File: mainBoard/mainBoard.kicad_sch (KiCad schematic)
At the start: 0 parts

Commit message: Added Stuff
Added Microcontroller, keyboard pins, voltage regulator, programming pins, and resonator.
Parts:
- added C1: 100nF, symbol Device:C_Small
- added C2, C6, C7: 10µF, symbol Device:C_Small
- added C4, C5: 22pF, symbol Device:C_Small
- added J2: Programmer, symbol Connector:Conn_01x05_Pin
- added J3: Keyboard, symbol Connector:Conn_01x05_Pin
- added U1: STM32G030K8Tx, Package_QFP:LQFP-32_7x7mm_P0.8mm, symbol MCU_ST_STM32G0:STM32G030K8Tx
- added U2: AMS1117-3.3, Package_TO_SOT_SMD:SOT-223-3_TabPin2, symbol Regulator_Linear:AMS1117-3.3
- added Y1: 48MHz, symbol Device:Crystal
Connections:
- new net: C4.2, U1.2 (PC14), Y1.2
- new net: C5.2, U1.3 (PC15), Y1.1
- new net +3V3: C1.1, C2.1, C6.1, J2.5 (Pin_5), J3.1 (Pin_1), U1.4 (VDD), U2.2 (VO)
- new net +5V: C7.1, U2.3 (VI)
- new net CS: J3.3 (Pin_3), U1.11 (PA4)
- new net GND: C1.2, C2.2, C4.1, C5.1, C6.2, C7.2, J2.1 (Pin_1), J3.5 (Pin_5), U1.5 (VSS), U2.1 (GND)
- new net MISO: J3.2 (Pin_2), U1.13 (PA6)
- new net RESET: J2.2 (Pin_2), U1.6 (NRST)
- new net SCLK: J3.4 (Pin_4), U1.12 (PA5)
- new net SWCLK: J2.3 (Pin_3), U1.25 (PA14)
- new net SWDIO: J2.4 (Pin_4), U1.24 (PA13)

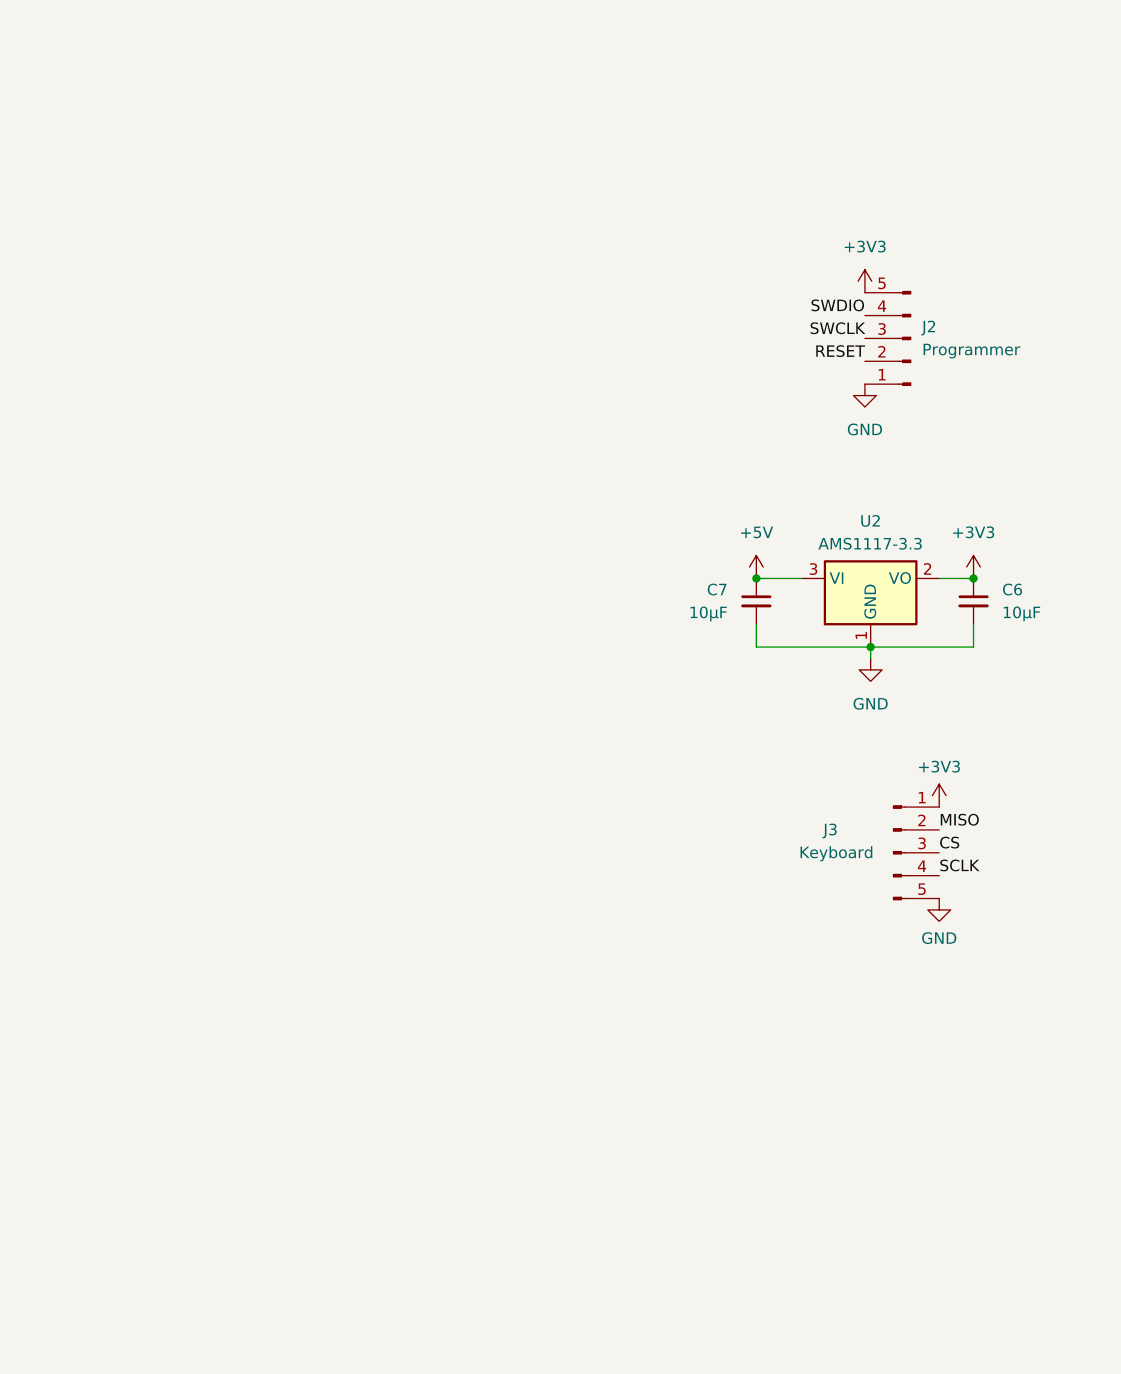
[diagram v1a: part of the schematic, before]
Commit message: Added Vibration Motor & NAND Flash
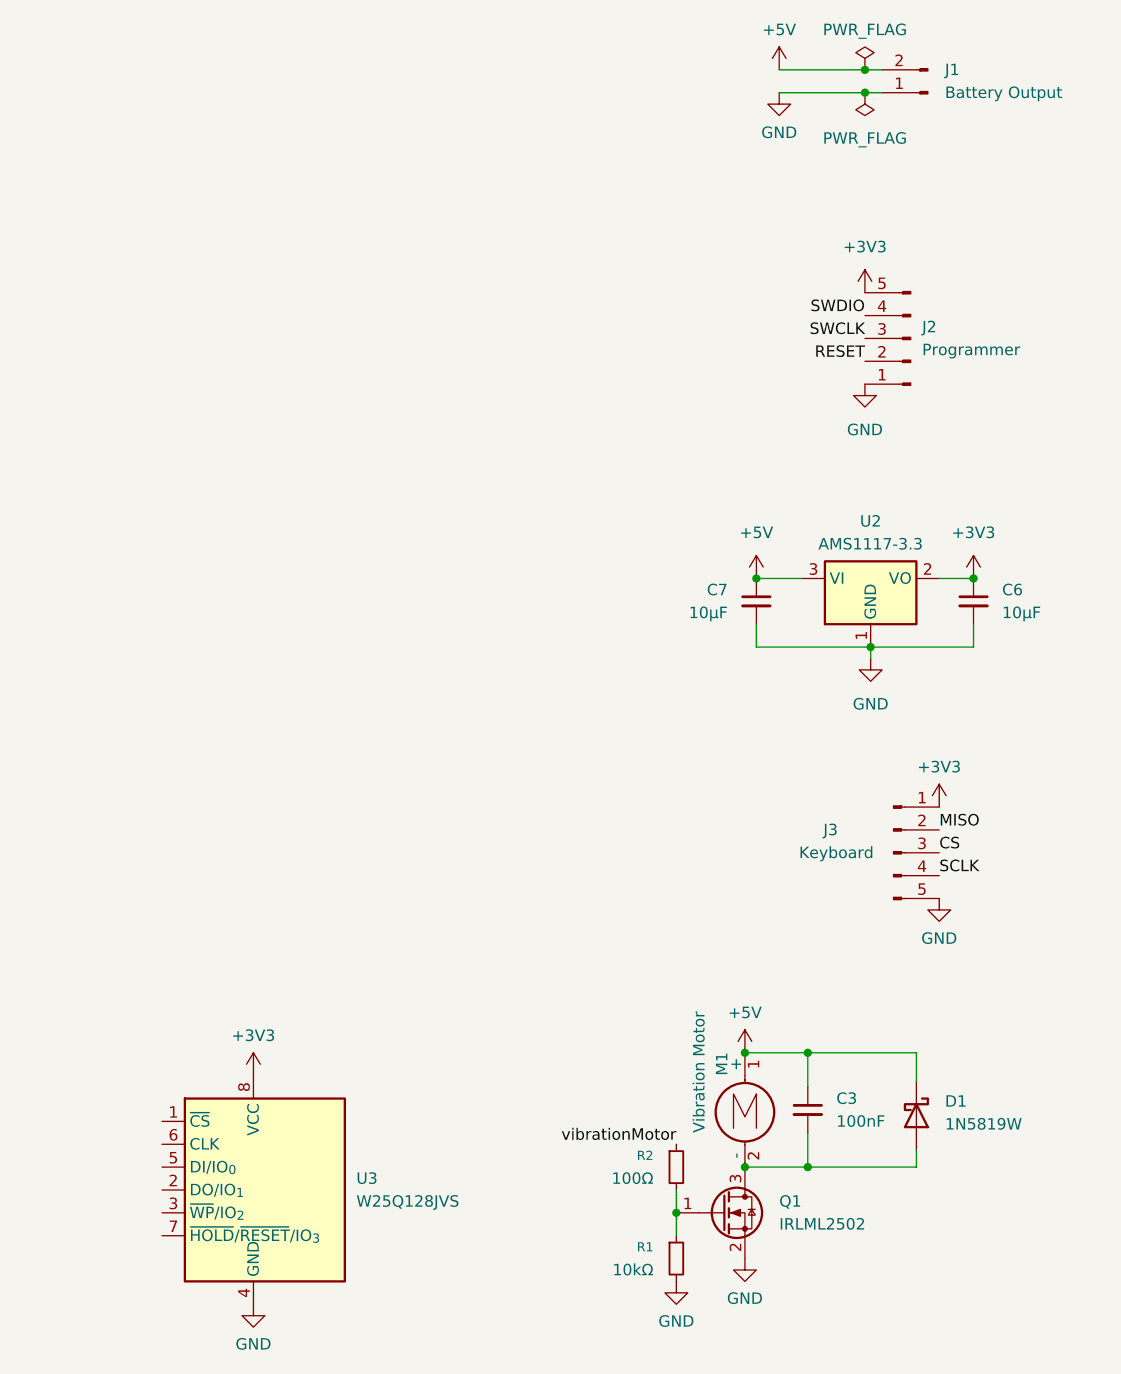
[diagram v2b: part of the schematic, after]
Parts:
- added C3: 100nF, symbol Device:C_Small
- added D1: 1N5819W, Diode_SMD:D_SOD-323_HandSoldering, symbol Diode:1N5819
- added J1: Battery Output, symbol Connector:Conn_01x02_Pin
- added M1: Vibration Motor, symbol Motor:Motor_DC
- added Q1: IRLML2502, Package_TO_SOT_SMD:SOT-23, symbol Transistor_FET:IRLML2060
- added R1: 10kΩ, symbol Device:R_Small
- added R2: 100Ω, symbol Device:R_Small
- added U3: W25Q128JVS, Package_SO:SOIC-8_5.3x5.3mm_P1.27mm, symbol Memory_Flash:W25Q128JVS
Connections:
- net +3V3: now also U3.8 (VCC)
- net +5V: now also C3.1, D1.1 (K), J1.2 (Pin_2), M1.1 (+)
- net GND: now also J1.1 (Pin_1), Q1.2 (S), R1.2, U3.4 (GND)
- new net: Q1.1 (G), R1.1, R2.2
- new net: C3.2, D1.2 (A), M1.2 (-), Q1.3 (D)
- new net vibrationMotor: R2.1

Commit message: Added Display
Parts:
- added C8: 100nF, symbol Device:C_Small
- added J4: display, symbol Connector:Conn_01x08_Pin
- added R3: 10kΩ, symbol Device:R_Small
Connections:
- net +3V3: now also C8.1, J4.2 (Pin_2), R3.1
- net GND: now also C8.2, J4.1 (Pin_1)
- net ~{CS2}: now reaches U1.1 (PB9)
- net ~{CS2}: now also U3.1 (~{CS})
- net displayRESET: now reaches U1.15 (PB0)
- net displayRESET: now also J4.5 (Pin_5)
- net BL: now reaches U1.16 (PB1)
- net BL: now also J4.8 (Pin_8)
- net DC: now reaches U1.17 (PB2)
- net DC: now also J4.6 (Pin_6)
- net CS3: now reaches U1.27 (PB3)
- net CS3: now also J4.7 (Pin_7)
- net ~{HOLD}: now reaches U1.28 (PB4)
- net ~{HOLD}: now also U3.7 (~{HOLD}/~{RESET}/IO_{3}), R3.2
- net ~{WP}: now reaches U1.29 (PB5)
- net ~{WP}: now also U3.3 (~{WP}/IO_{2})
- net MISO2: now reaches U1.30 (PB6)
- net MISO2: now also U3.2 (DO/IO_{1})
- net MOSI2: now reaches U1.31 (PB7)
- net MOSI2: now also U3.5 (DI/IO_{0}), J4.4 (Pin_4)
- net SCLK2: now reaches U1.32 (PB8)
- net SCLK2: now also U3.6 (CLK), J4.3 (Pin_3)

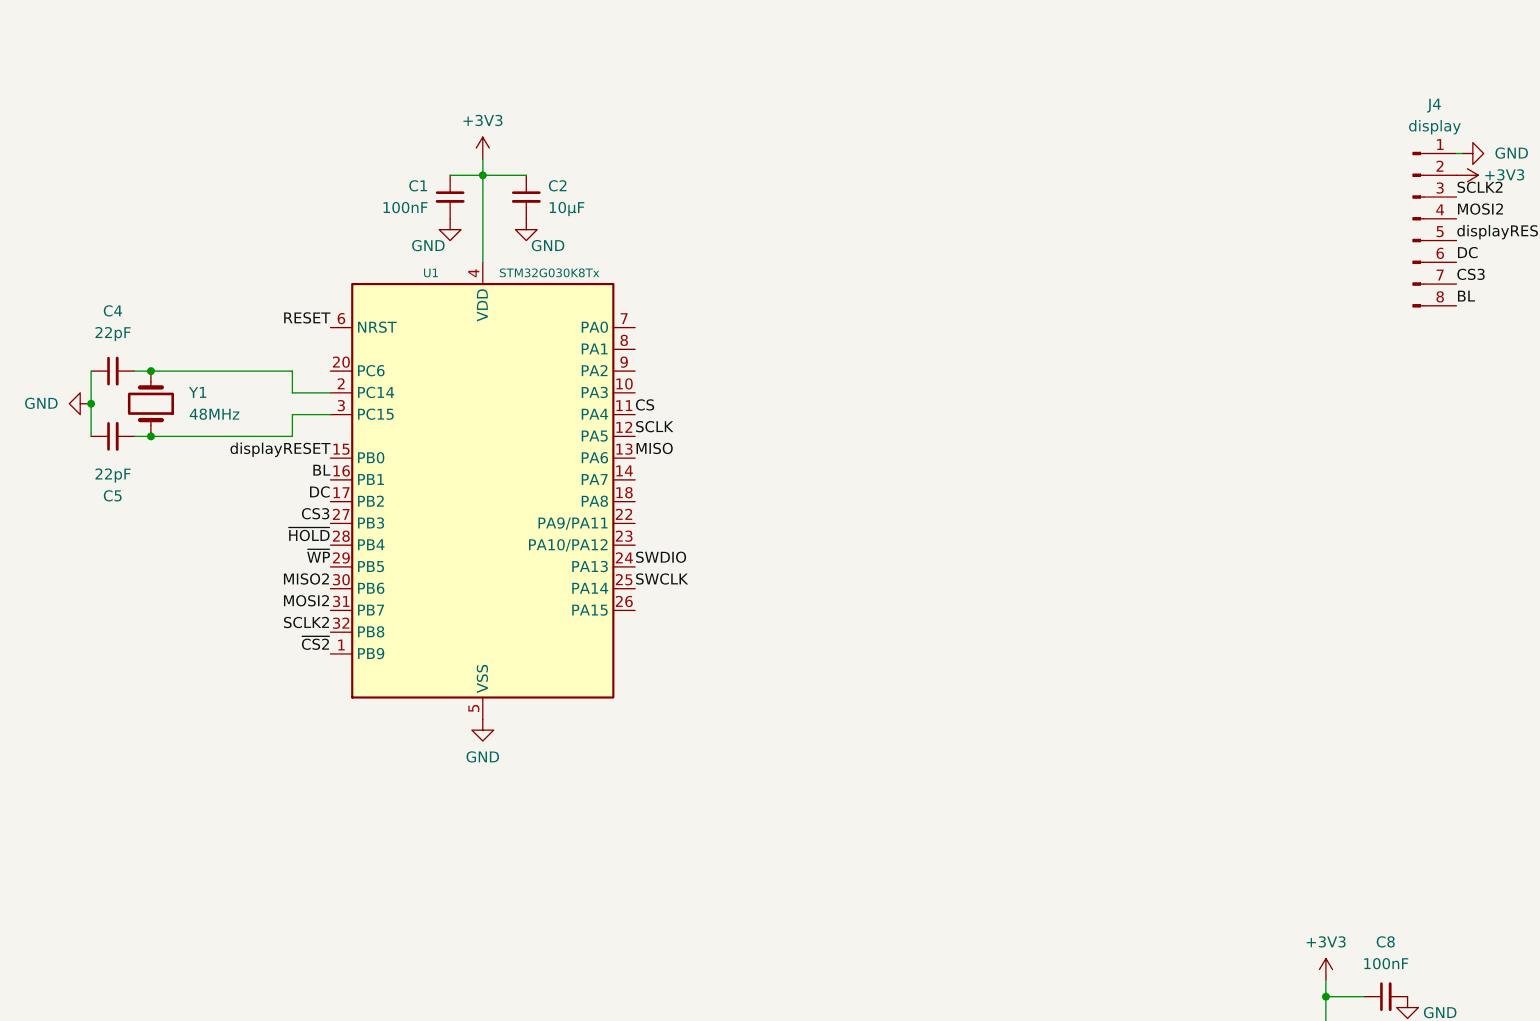
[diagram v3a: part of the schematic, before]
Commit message: Connected Vibration Motor to MCU
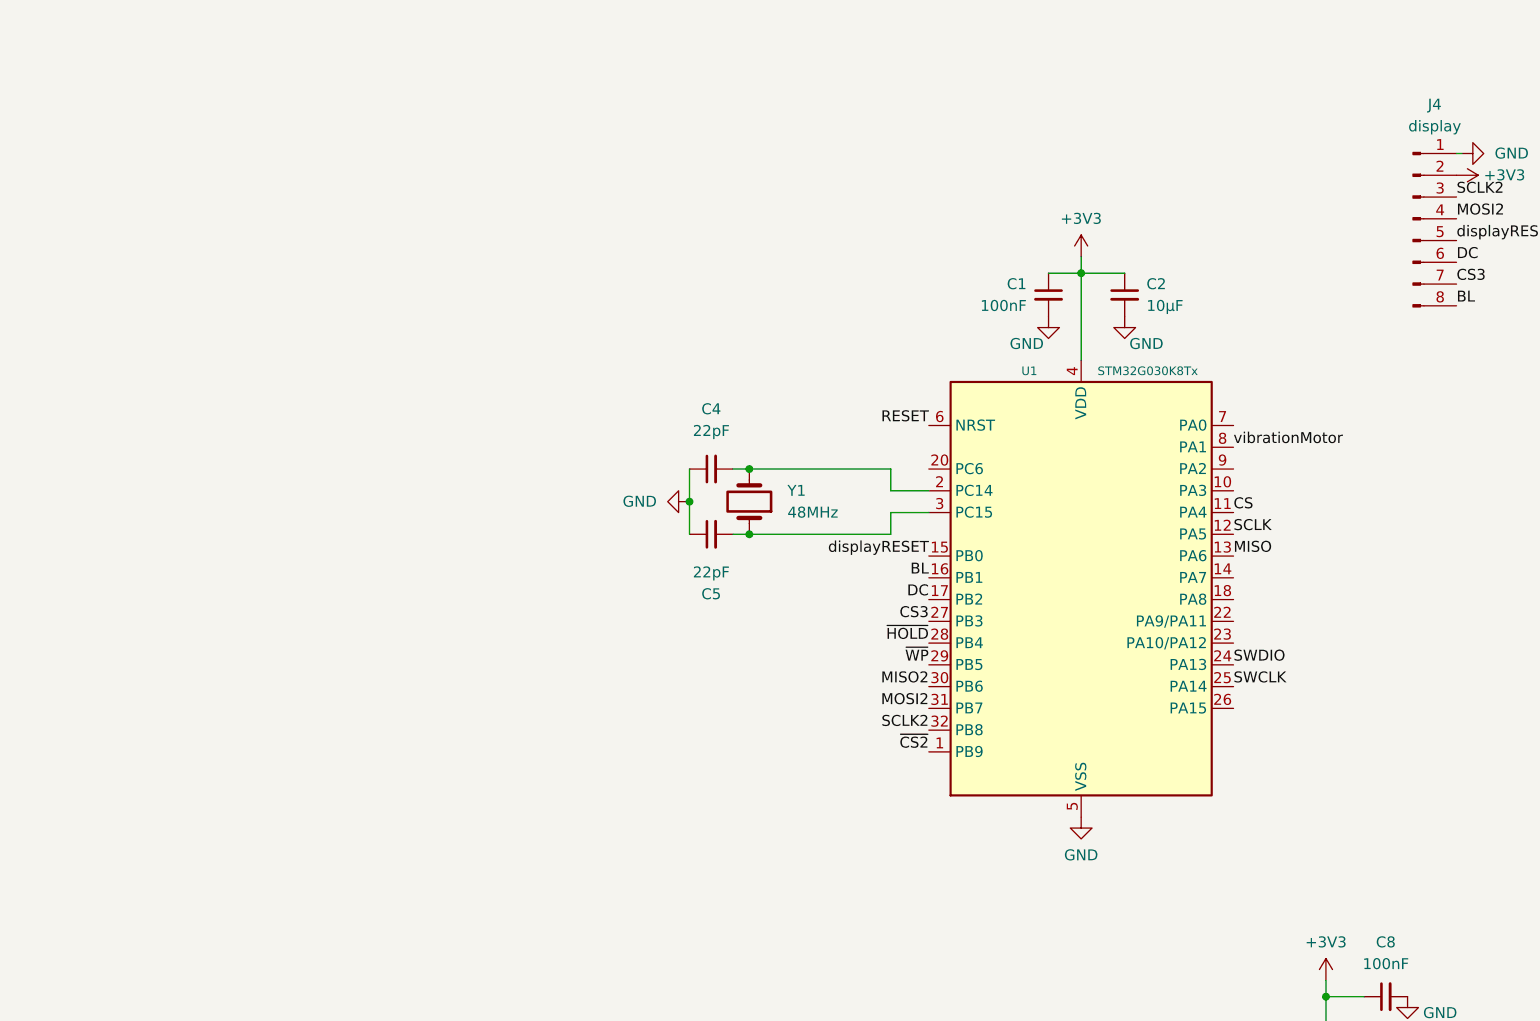
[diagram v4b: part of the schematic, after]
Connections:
- net vibrationMotor: now also U1.8 (PA1)
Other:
- moved on the sheet: C1, C2, C4, C5, U1, Y1
